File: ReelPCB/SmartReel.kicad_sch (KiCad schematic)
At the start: 10 parts, among them CN1 M3 Solder Nut, CN2 M3 Solder Nut, CN3 M3 Solder Nut, J1 8 pin header, J2 8 pin socket

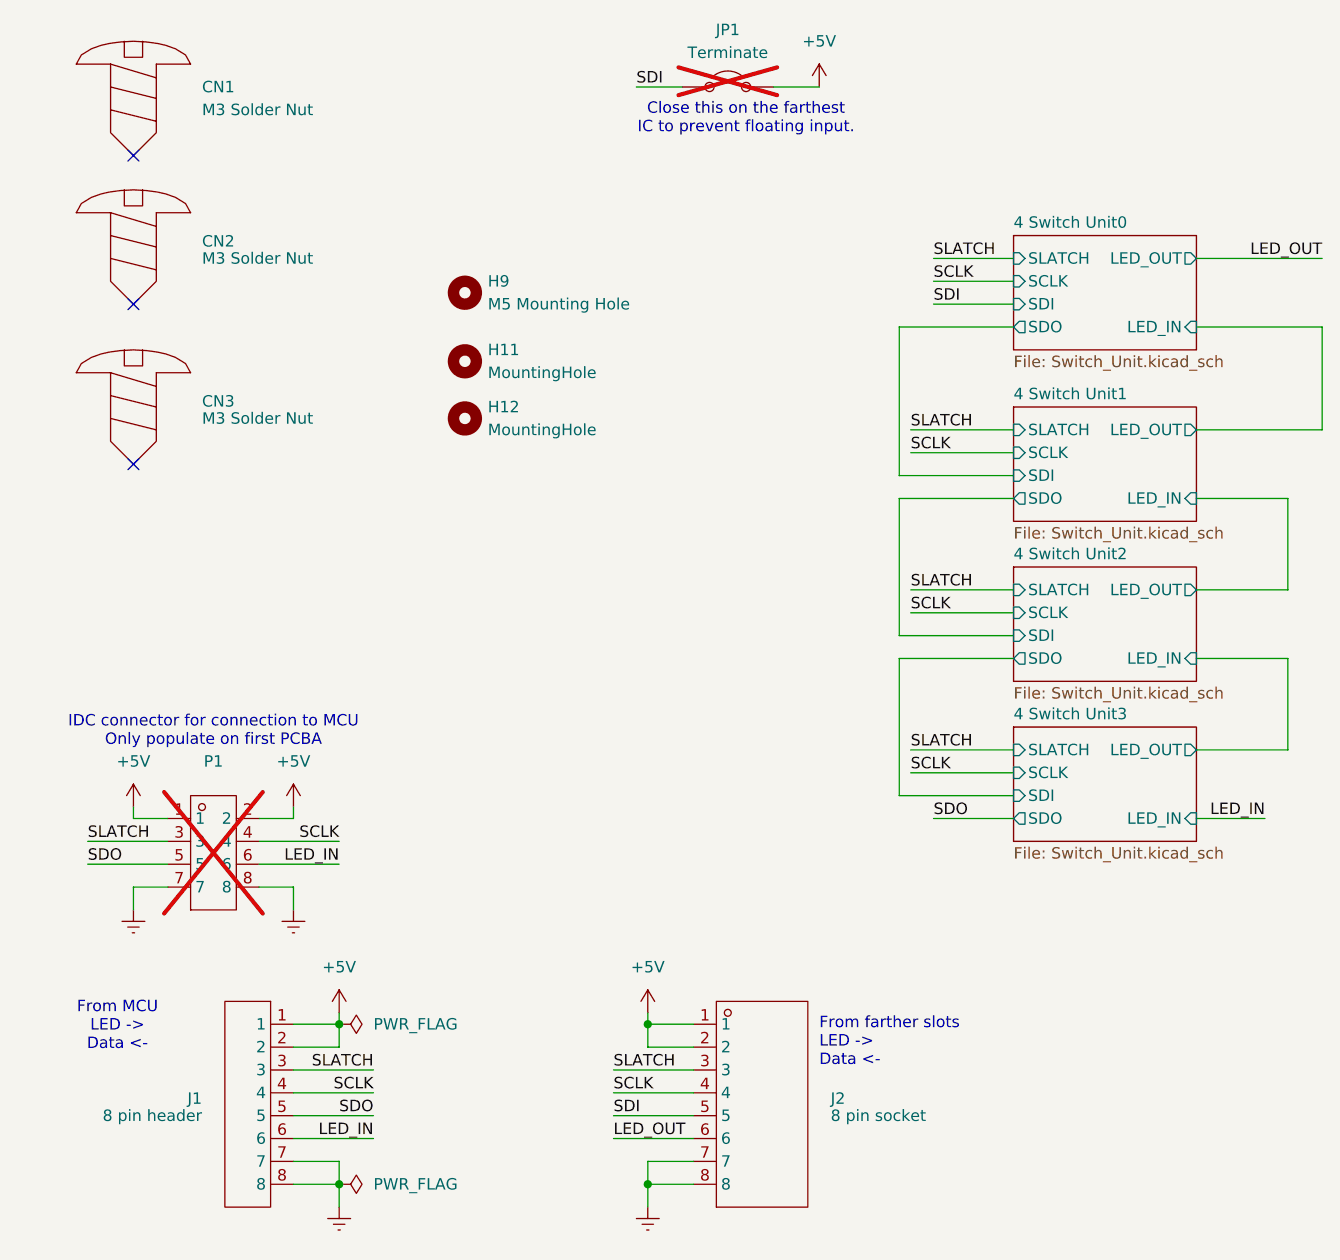
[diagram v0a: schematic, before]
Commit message: Move files and route reel PCB
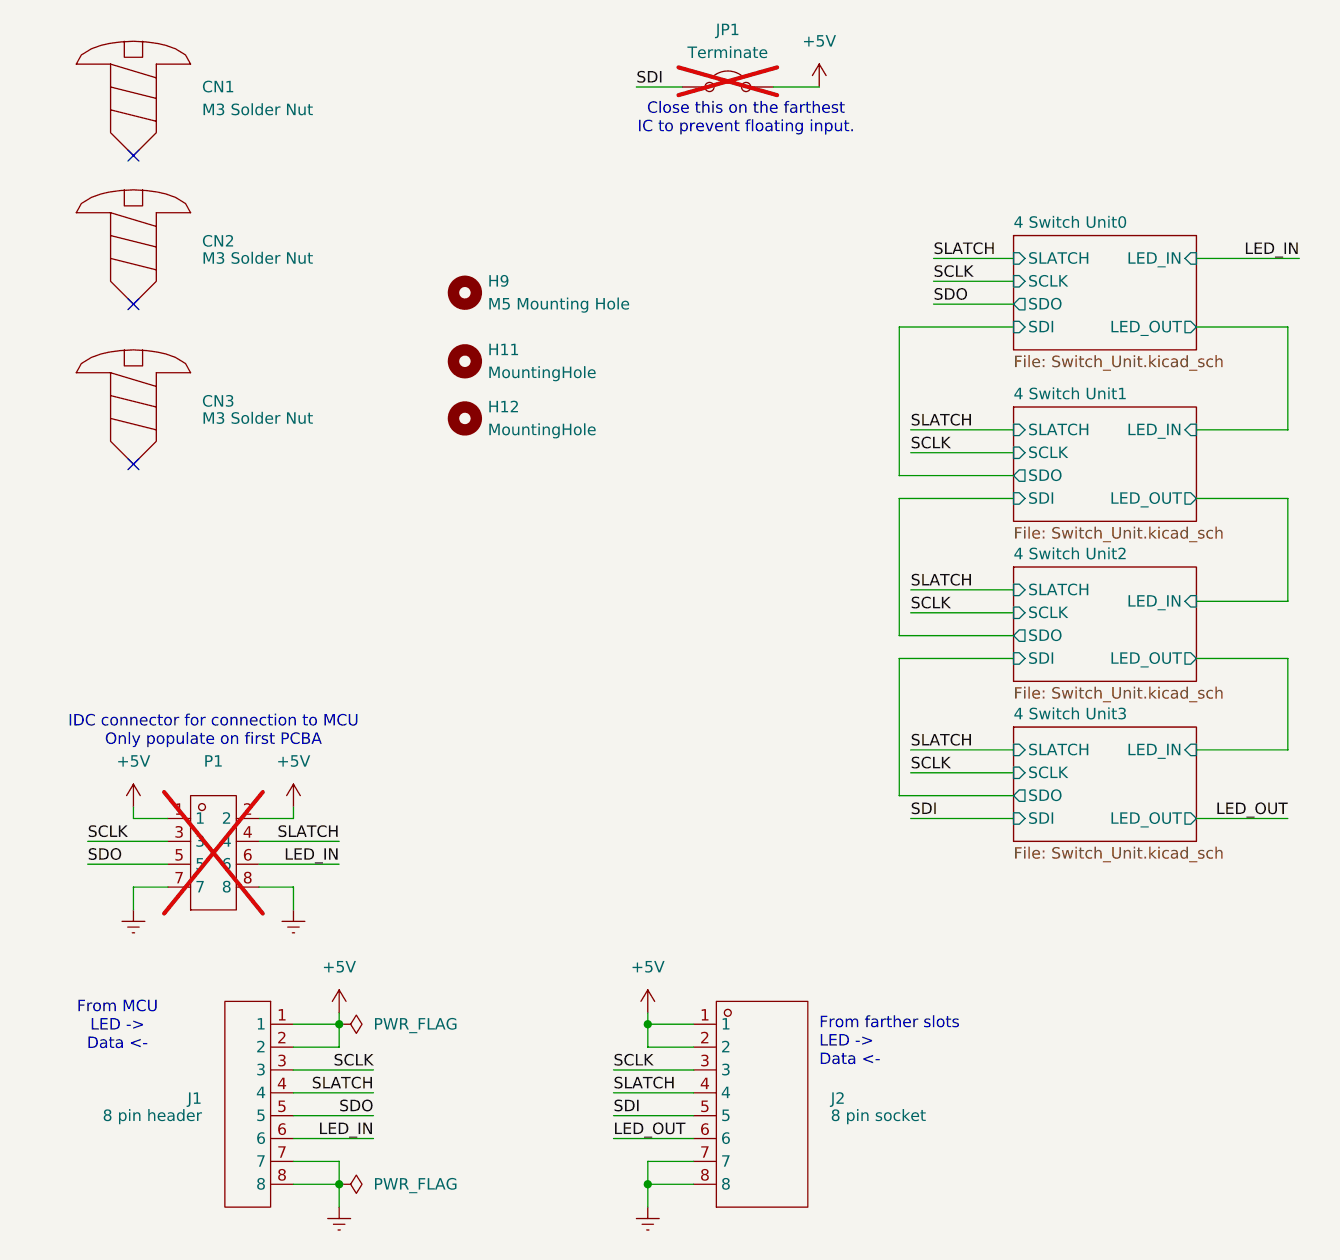
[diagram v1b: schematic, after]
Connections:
- net SCLK: now also J1.3, J2.3, P1.3; no longer J1.4, J2.4, P1.4
- net SLATCH: now also J1.4, J2.4, P1.4; no longer J1.3, J2.3, P1.3

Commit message: Rev 1 PCBs ordered
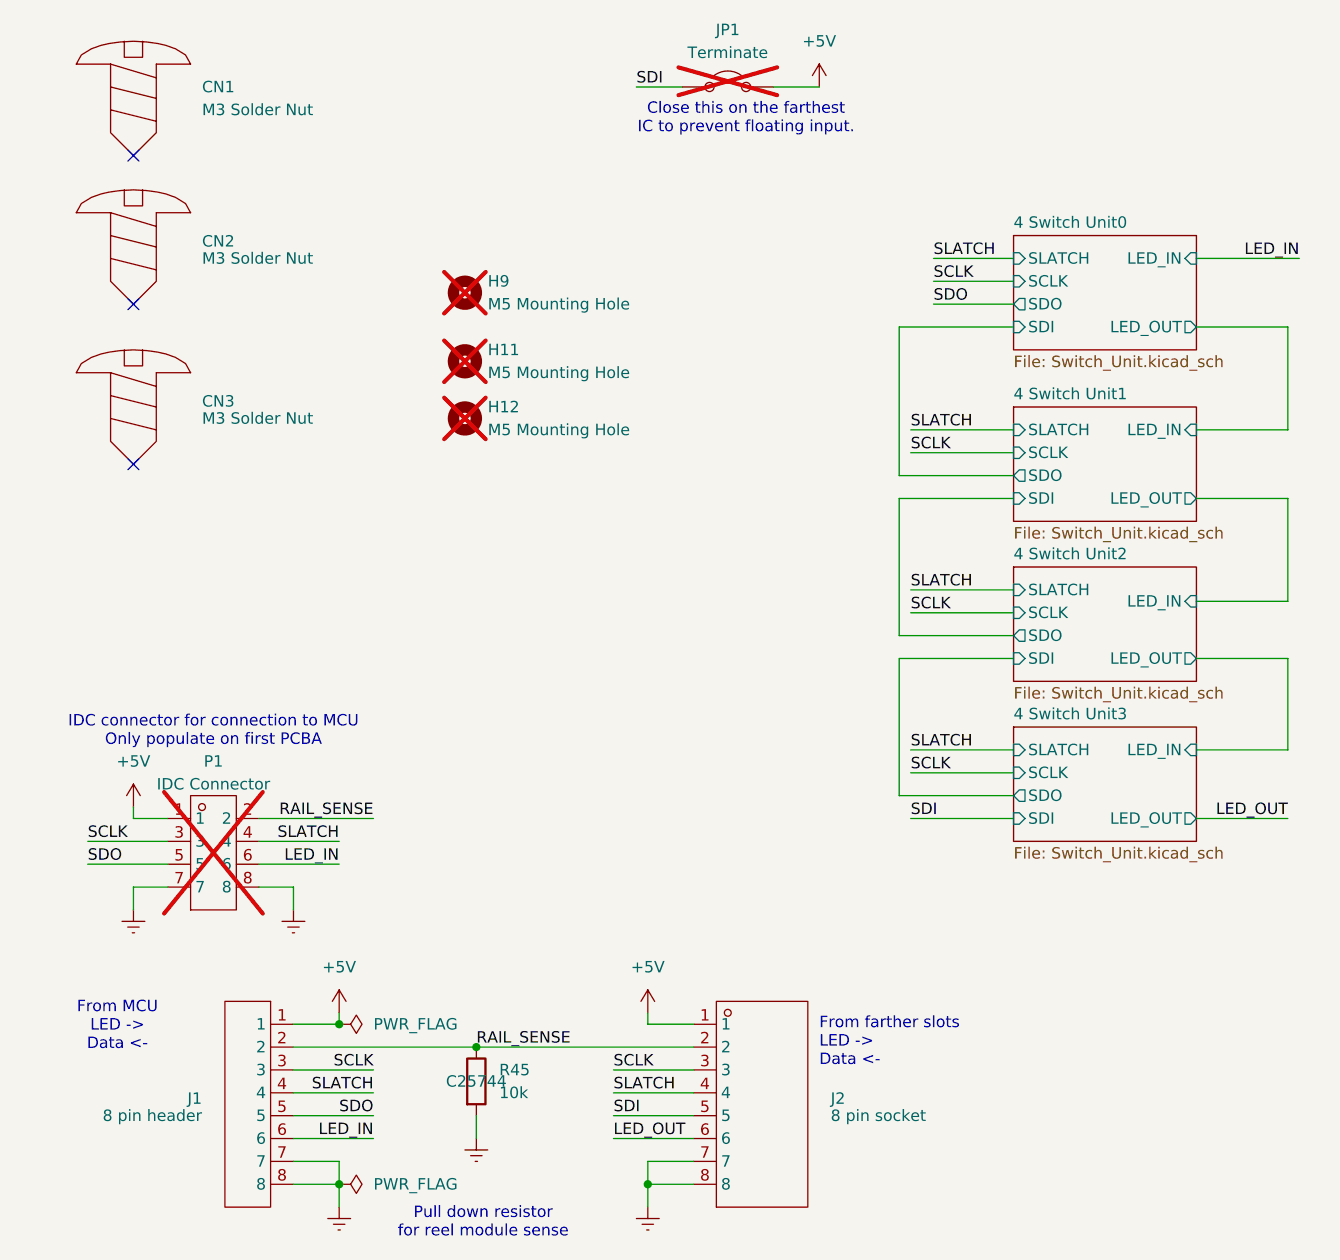
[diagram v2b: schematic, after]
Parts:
- added R45: 10k, Resistor_SMD:R_0402_1005Metric, symbol Device:R
- H11, H12: value MountingHole -> M5 Mounting Hole; now not fitted
- H9: now not fitted
- P1: value ~ -> IDC Connector
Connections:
- net +5V: no longer J1.2, J2.2, P1.2
- net Earth: now also R45.2
- new net RAIL_SENSE: J1.2, J2.2, P1.2, R45.1
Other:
- note added: "Pull down resistor for reel module sense"
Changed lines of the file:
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@@
+		)
+	)
+	(text "Pull down resistor\nfor reel module sense"
+		(exclude_from_sim no)
+		(at 68.072 150.368 0)
+		(effects
+			(font
+				(size 1.27 1.27)
+			)
 		)
 	)
@@
 			(justify left)
 		)
-	)
-	(junction
-		(at 86.36 128.27)
-		(diameter 0)
-		(color 0 0 0 0)
 	)
 	(junction
@@
 	)
 	(junction
+		(at 67.31 130.81)
+		(diameter 0)
+		(color 0 0 0 0)
+	)
+	(junction
 		(at 52.07 146.05)
 		(diameter 0)
@@
 	(wire
 		(pts
-			(xy 46.99 105.41) (xy 46.99 104.14)
-		)
-		(stroke
-			(width 0)
-			(type default)
-		)
-	)
-	(wire
-		(pts
 			(xy 52.07 107.95) (xy 43.18 107.95)
 		)
@@
 	(wire
 		(pts
-			(xy 86.36 130.81) (xy 91.44 130.81)
-		)
-		(stroke
-			(width 0)
-			(type default)
-		)
-	)
-	(wire
-		(pts
 			(xy 115.57 100.33) (xy 127 100.33)
 		)
@@
 	(wire
 		(pts
+			(xy 67.31 130.81) (xy 91.44 130.81)
+		)
+		(stroke
+			(width 0)
+			(type default)
+		)
+	)
+	(wire
+		(pts
 			(xy 100.33 24.13) (xy 105.41 24.13)
 		)
@@
 	(wire
 		(pts
+			(xy 67.31 138.43) (xy 67.31 140.97)
+		)
+		(stroke
+			(width 0)
+			(type default)
+		)
+	)
+	(wire
+		(pts
 			(xy 127 45.72) (xy 118.11 45.72)
 		)
@@
 	(wire
 		(pts
-			(xy 52.07 128.27) (xy 52.07 130.81)
-		)
-		(stroke
-			(width 0)
-			(type default)
-		)
-	)
-	(wire
-		(pts
 			(xy 115.57 82.55) (xy 127 82.55)
 		)
@@
 	(wire
 		(pts
-			(xy 52.07 130.81) (xy 46.99 130.81)
-		)
-		(stroke
-			(width 0)
-			(type default)
-		)
-	)
-	(wire
-		(pts
-			(xy 43.18 105.41) (xy 46.99 105.41)
+			(xy 46.99 130.81) (xy 67.31 130.81)
+		)
+		(stroke
+			(width 0)
+			(type default)
+		)
+	)
+	(wire
+		(pts
+			(xy 43.18 105.41) (xy 55.88 105.41)
 		)
 		(stroke
@@
 		(pts
 			(xy 157.48 62.23) (xy 147.32 62.23)
-		)
-		(stroke
-			(width 0)
-			(type default)
-		)
-	)
-	(wire
-		(pts
-			(xy 86.36 128.27) (xy 86.36 130.81)
 		)
 		(stroke
@@
 		)
 	)
+	(label "RAIL_SENSE"
+		(at 55.88 105.41 180)
+		(effects
+			(font
+				(size 1.27 1.27)
+			)
+			(justify right bottom)
+		)
+	)
 	(label "SDO"
 		(at 24.13 110.49 0)
@@
 			)
 			(justify right bottom)
+		)
+	)
+	(label "RAIL_SENSE"
+		(at 67.31 130.81 0)
+		(effects
+			(font
+				(size 1.27 1.27)
+			)
+			(justify left bottom)
 		)
 	)
@@
 		(in_bom no)
 		(on_board yes)
-		(dnp no)
+		(dnp yes)
 		(fields_autoplaced yes)
 		(property "Reference" "H12"
@@
 			)
 		)
-		(property "Value" "MountingHole"
+		(property "Value" "M5 Mounting Hole"
 			(at 68.58 62.2299 0)
 			(effects
@@
 	)
 	(symbol
-		(lib_id "power:+5V")
-		(at 46.99 104.14 0)
-		(mirror y)
+		(lib_id "Device:R")
+		(at 67.31 134.62 0)
 		(unit 1)
 		(exclude_from_sim no)
@@
 		(dnp no)
 		(fields_autoplaced yes)
-		(property "Reference" "#PWR053"
-			(at 46.99 107.95 0)
-			(effects
-				(font
-					(size 1.27 1.27)
-				)
-				(hide yes)
-			)
-		)
-		(property "Value" "+5V"
-			(at 46.99 99.06 0)
-			(effects
-				(font
-					(size 1.27 1.27)
-				)
-			)
-		)
-		(property "Footprint" ""
-			(at 46.99 104.14 0)
-			(effects
-				(font
-					(size 1.27 1.27)
-				)
-				(hide yes)
-			)
-		)
-		(property "Datasheet" ""
-			(at 46.99 104.14 0)
-			(effects
-				(font
-					(size 1.27 1.27)
-				)
-				(hide yes)
-			)
-		)
-		(property "Description" "Power symbol creates a global label with name \"+5V\""
-			(at 46.99 104.14 0)
-			(effects
-				(font
-					(size 1.27 1.27)
-				)
-				(hide yes)
-			)
+		(property "Reference" "R45"
+			(at 69.85 133.3499 0)
+			(effects
+				(font
+					(size 1.27 1.27)
+				)
+				(justify left)
+			)
+		)
+		(property "Value" "10k"
+			(at 69.85 135.8899 0)
+			(effects
+				(font
+					(size 1.27 1.27)
+				)
+				(justify left)
+			)
+		)
+		(property "Footprint" "Resistor_SMD:R_0402_1005Metric"
+			(at 65.532 134.62 90)
+			(effects
+				(font
+					(size 1.27 1.27)
+				)
+				(hide yes)
+			)
+		)
+		(property "Datasheet" "~"
+			(at 67.31 134.62 0)
+			(effects
+				(font
+					(size 1.27 1.27)
+				)
+				(hide yes)
+			)
+		)
+		(property "Description" "Resistor"
+			(at 67.31 134.62 0)
+			(effects
+				(font
+					(size 1.27 1.27)
+				)
+				(hide yes)
+			)
+		)
+		(property "Supplier Part" "C25744"
+			(at 67.31 134.62 0)
+			(effects
+				(font
+					(size 1.27 1.27)
+				)
+			)
+		)
+		(pin "2"
 		)
 		(pin "1"
@@
 			(project "SmartReel"
 				(path "/aed789a4-0b23-43bd-bf60-387cb49d3e4c"
-					(reference "#PWR053")
+					(reference "R45")
 					(unit 1)
 				)
@@
 	(symbol
 		(lib_id "power:Earth")
+		(at 67.31 140.97 0)
+		(mirror y)
+		(unit 1)
+		(exclude_from_sim no)
+		(in_bom yes)
+		(on_board yes)
+		(dnp no)
+		(fields_autoplaced yes)
+		(property "Reference" "#PWR062"
+			(at 67.31 147.32 0)
+			(effects
+				(font
+					(size 1.27 1.27)
+				)
+				(hide yes)
+			)
+		)
+		(property "Value" "Earth"
+			(at 67.31 146.05 0)
+			(effects
+				(font
+					(size 1.27 1.27)
+				)
+				(hide yes)
+			)
+		)
+		(property "Footprint" ""
+			(at 67.31 140.97 0)
+			(effects
+				(font
+					(size 1.27 1.27)
+				)
+				(hide yes)
+			)
+		)
+		(property "Datasheet" "~"
+			(at 67.31 140.97 0)
+			(effects
+				(font
+					(size 1.27 1.27)
+				)
+				(hide yes)
+			)
+		)
+		(property "Description" "Power symbol creates a global label with name \"Earth\""
+			(at 67.31 140.97 0)
+			(effects
+				(font
+					(size 1.27 1.27)
+				)
+				(hide yes)
+			)
+		)
+		(pin "1"
+		)
+		(instances
+			(project "SmartReel"
+				(path "/aed789a4-0b23-43bd-bf60-387cb49d3e4c"
+					(reference "#PWR062")
+					(unit 1)
+				)
+			)
+		)
+	)
+	(symbol
+		(lib_id "power:Earth")
 		(at 29.21 115.57 0)
 		(mirror y)
@@
 		(in_bom no)
 		(on_board yes)
-		(dnp no)
+		(dnp yes)
 		(fields_autoplaced yes)
 		(property "Reference" "H11"
@@
 			)
 		)
-		(property "Value" "MountingHole"
+		(property "Value" "M5 Mounting Hole"
 			(at 68.58 55.8799 0)
 			(effects
@@
 			)
 		)
-		(property "Value" "~"
+		(property "Value" "IDC Connector"
 			(at 38.1 101.6 0)
 			(effects
@@
 		(in_bom no)
 		(on_board yes)
-		(dnp no)
+		(dnp yes)
 		(fields_autoplaced yes)
 		(property "Reference" "H9"
